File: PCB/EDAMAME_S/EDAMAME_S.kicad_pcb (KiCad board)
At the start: 2 copper layers, 75 x 96 mm, 73 parts, among them CN1 USB-B-MICRO, J1 Conn, J2 ISP, J3 Conn, J4 Nichrome, M1 Motor_L, M2 Motor_R, Q1 MTM231102LBF, Q2 2SC2712, SW1 power, U1 microSD, U2 ATMEGA1284P-MU, U3 LSM303C, U4 TPS63001, U5 GYSFDMAXB, U6 FT231XQ, U7 BD6211F, U8 INA226, U9 BD6211F, Y1 16MHz

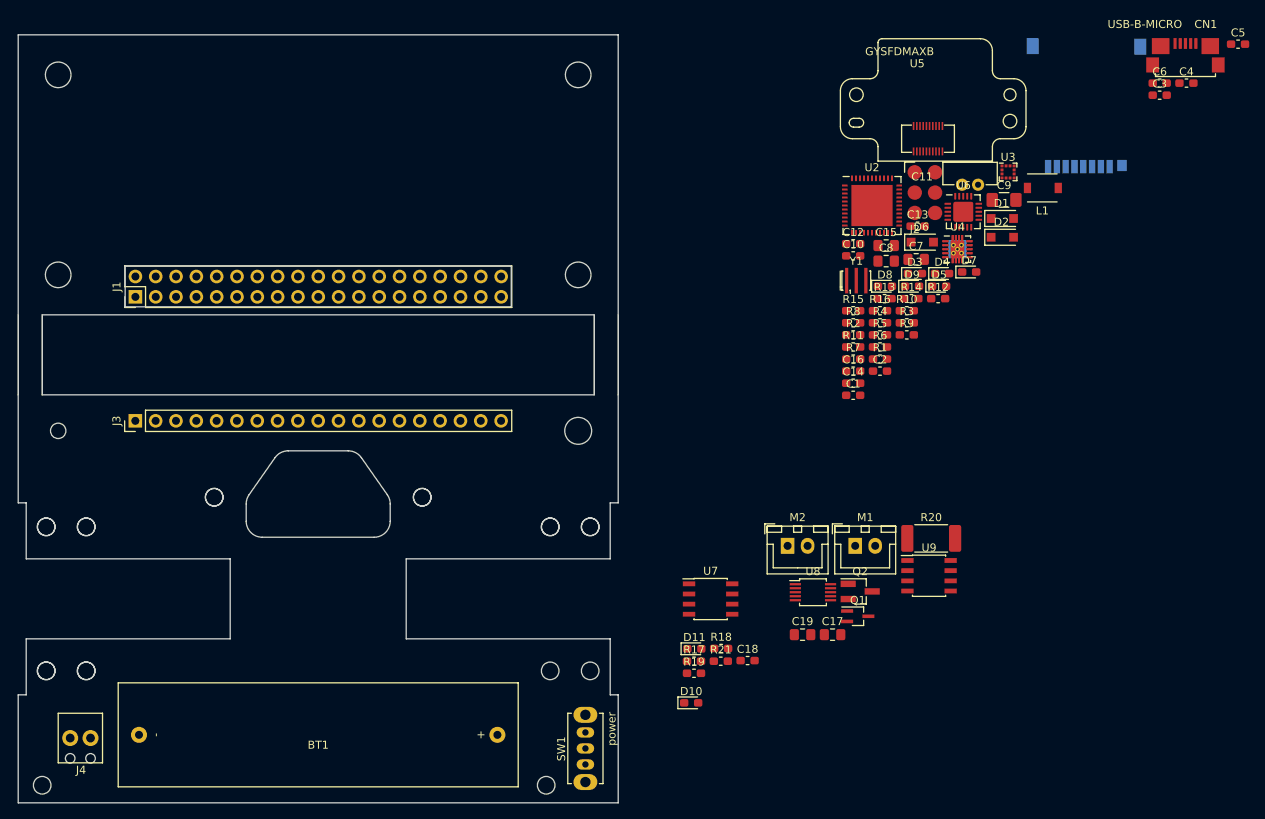
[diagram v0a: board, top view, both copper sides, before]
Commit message: えだまめS 基板更新
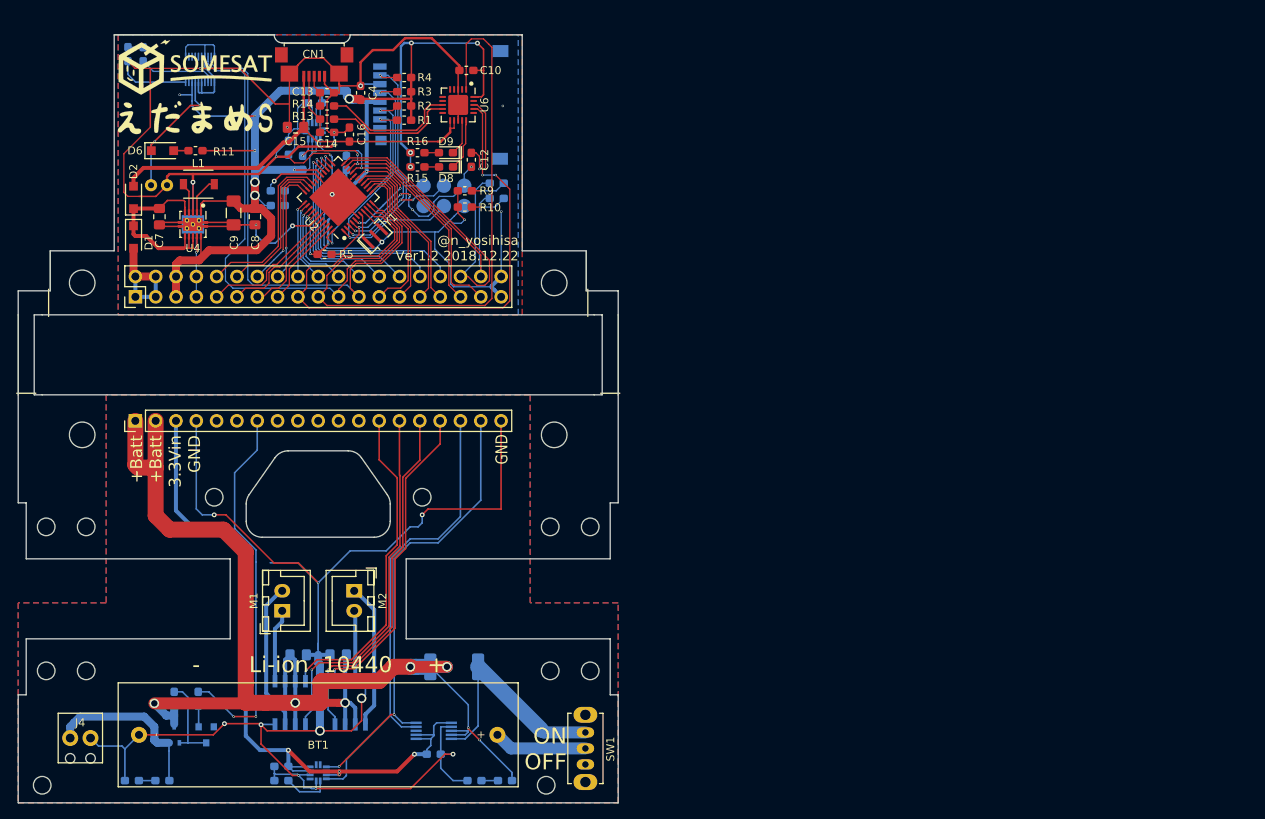
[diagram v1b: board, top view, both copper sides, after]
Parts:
- removed C1: 0.1u, Capacitor_SMD:C_0603_1608Metric_Pad1.05x0.95mm_HandSolder
- added C20: 0.1u, Capacitor_SMD:C_0603_1608Metric_Pad1.05x0.95mm_HandSolder, B.Cu at (61.4, 108.6)
- added C21: 0.1u, Capacitor_SMD:C_0603_1608Metric_Pad1.05x0.95mm_HandSolder, B.Cu at (61.4, 110.4)
- added G***: LOGO, logo:SOMESAT_edamame_s_logo, F.Cu at (50.6, 24.0)
- added G***: LOGO, logo:SOMESAT_logo, B.Cu at (83.5, 70.6)
- added U10: LSM303C, user:LGA-12_2x2mm_P0.5mm_HandSolder, B.Cu at (66.1, 109.4)
- C11, C18, C2, C3, C5, C6, D10, D11, D3, D4, D5, D7, J2, R12, R17, R18, R19, R20, R21, R6, R7, R8, U5, U8: moved to B.Cu
- C17: renamed from C19; moved to B.Cu
- C19: renamed from C17; moved to B.Cu
- M1: renamed from M2; value Motor_R -> Motor_L
- M2: renamed from M1; value Motor_L -> Motor_R
- Q1: footprint Package_TO_SOT_SMD:SOT-323_SC-70_Handsoldering -> Package_TO_SOT_SMD:SOT-323_SC-70; moved to B.Cu
- Q2: footprint Package_TO_SOT_SMD:SOT-23_Handsoldering -> Package_TO_SOT_SMD:SOT-23; moved to B.Cu
- U3: footprint Package_LGA:LGA-12_2x2mm_P0.5mm -> user:LGA-12_2x2mm_P0.5mm_HandSolder; moved to B.Cu
- U4: footprint Package_SON:Texas_S-PWSON-N10_ThermalVias -> Package_SON:Texas_S-PVSON-N10_ThermalVias
- U7: renamed from U9; moved to B.Cu
- U9: renamed from U7; moved to B.Cu
- Y1: footprint Crystal:Resonator_SMD_muRata_CSTxExxV-3Pin_3.0x1.1mm_HandSoldering -> Crystal:Resonator_SMD_muRata_CSTxExxV-3Pin_3.0x1.1mm
- moved C5 115.6 mm to (65.6, 25.7), turned to 180 degrees
- moved C6 109.2 mm to (62.3, 31.3), turned to 90 degrees
- moved CN1 108.9 mm to (65.6, 19.7), turned to 180 degrees
- moved D2 108.7 mm to (43.0, 37.5), turned to 90 degrees
- moved D1 108.6 mm to (43.0, 42.4), turned to 270 degrees
- moved D7 108.6 mm to (42.3, 19.6), turned to 90 degrees
- moved L1 105.5 mm to (51.1, 35.8)
- moved R12 104.0 mm to (44.2, 19.6), turned to 270 degrees
- moved C3 103.4 mm to (68.7, 38.1), turned to 180 degrees
- moved C4 103.2 mm to (71.4, 24.4), turned to 90 degrees
- moved C11 101.4 mm to (46.2, 36.0)
- moved C9 96.3 mm to (55.5, 39.4), turned to 270 degrees
- moved D6 95.7 mm to (46.6, 31.6)
- moved U4 95.6 mm to (50.4, 40.8), turned to 270 degrees
- moved C7 94.7 mm to (46.2, 39.9), turned to 270 degrees
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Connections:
- C14 pad 1: Net-(C13-Pad1) -> Net-(C14-Pad1)
- CN1 pad 2: Net-(C13-Pad1) -> Net-(C14-Pad1)
- CN1 pad 3: Net-(CN1-Pad3) -> Net-(C13-Pad1)
- CN1 pad 4: Net-(CN1-Pad4) -> (no net)
- D4 pad 1: GND -> Net-(D4-Pad1)
- D4 pad 2: Net-(D4-Pad2) -> /EDAMAME_S_core/19
- D5 pad 1: GND -> Net-(D5-Pad1)
- D5 pad 2: Net-(D5-Pad2) -> /EDAMAME_S_core/18
- J1 pad 1: Net-(J1-Pad1) -> Net-(D1-Pad2)
- J1 pad 10: /EDAMAME_S_core/18 -> /EDAMAME_S_core/A7
- J1 pad 12: /EDAMAME_S_core/19 -> /EDAMAME_S_core/A6
- J1 pad 14: /EDAMAME_S_core/20 -> /EDAMAME_S_core/A5
- J1 pad 16: /EDAMAME_S_core/21 -> /EDAMAME_S_core/A4
- J1 pad 18: /EDAMAME_S_core/22 -> /EDAMAME_S_core/A3
- J1 pad 20: /EDAMAME_S_core/23 -> /EDAMAME_S_core/A2
- J1 pad 22: /EDAMAME_S_core/A0 -> /EDAMAME_S_core/A1
- J1 pad 24: /EDAMAME_S_core/A1 -> /EDAMAME_S_core/A0
- J1 pad 26: /EDAMAME_S_core/A2 -> /EDAMAME_S_core/23
- J1 pad 28: /EDAMAME_S_core/A3 -> /EDAMAME_S_core/22
- J1 pad 3: Net-(J1-Pad1) -> Net-(D1-Pad2)
- J1 pad 30: /EDAMAME_S_core/A4 -> /EDAMAME_S_core/21
- J1 pad 32: /EDAMAME_S_core/A5 -> /EDAMAME_S_core/20
- J1 pad 34: /EDAMAME_S_core/A6 -> /EDAMAME_S_core/19
- J1 pad 36: /EDAMAME_S_core/A7 -> /EDAMAME_S_core/18
- J2 pad 2: +3V3 -> (no net)
- J3 pad 10: Net-(J3-Pad10) -> (no net)
- J3 pad 11: Net-(J3-Pad11) -> (no net)
- J3 pad 12: Net-(J3-Pad12) -> (no net)
- J3 pad 5: Net-(J3-Pad5) -> (no net)
- J3 pad 6: Net-(J3-Pad6) -> (no net)
- J3 pad 8: Net-(J3-Pad8) -> (no net)
- J3 pad 9: Net-(J3-Pad9) -> (no net)
- R10 pad 1: /EDAMAME_S_core/18 -> Net-(D5-Pad1)
- R10 pad 2: Net-(D5-Pad2) -> GND
- R13 pad 2: Net-(C13-Pad1) -> Net-(C14-Pad1)
- R14 pad 2: Net-(CN1-Pad3) -> Net-(C13-Pad1)
- R9 pad 1: /EDAMAME_S_core/19 -> Net-(D4-Pad1)
- R9 pad 2: Net-(D4-Pad2) -> GND
- U1 pad 1: Net-(U1-Pad1) -> (no net)
- U1 pad 8: Net-(U1-Pad8) -> (no net)
- U2 pad 29: Net-(U2-Pad29) -> (no net)
- U2 pad 45: (no net) -> GND
- U3 pad 11: Net-(U3-Pad11) -> (no net)
- U3 pad 12: Net-(U3-Pad12) -> (no net)
- U3 pad 7: Net-(U3-Pad7) -> (no net)
- U5 pad 4: Net-(U5-Pad4) -> (no net)
- U6 pad 10: Net-(U6-Pad10) -> (no net)
- U6 pad 16: Net-(U6-Pad16) -> (no net)
- U6 pad 19: Net-(U6-Pad19) -> (no net)
- U6 pad 2: Net-(U6-Pad2) -> (no net)
- U6 pad 4: Net-(U6-Pad4) -> (no net)
- U6 pad 5: Net-(U6-Pad5) -> (no net)
- U6 pad 6: Net-(U6-Pad6) -> (no net)
- U6 pad 7: Net-(U6-Pad7) -> (no net)
- U7 pad 4: /EDAMAME_S_Ex/MOTOR_RR -> /EDAMAME_S_Ex/MOTOR_LF
- U7 pad 5: /EDAMAME_S_Ex/MOTOR_RF -> /EDAMAME_S_Ex/MOTOR_LR
- U8 pad 3: Net-(U8-Pad3) -> (no net)
- U9 pad 4: /EDAMAME_S_Ex/MOTOR_LF -> /EDAMAME_S_Ex/MOTOR_RR
- U9 pad 5: /EDAMAME_S_Ex/MOTOR_LR -> /EDAMAME_S_Ex/MOTOR_RF
- Y1 pad 2: Net-(Y1-Pad2) -> GND
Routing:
- net GND: track 0.00 -> 313.1 mm, vias 0 -> 18
- net +3V3: track 0.00 -> 207.7 mm, vias 0 -> 18
- net GNDPWR: track 0.00 -> 195.7 mm, vias 0 -> 10
- net +BATT: track 0.00 -> 159.3 mm, vias 0 -> 7
- net VCC: track 0.00 -> 92.1 mm, vias 0 -> 4
- net /EDAMAME_S_core/AVR→PC: track 0.00 -> 83.5 mm
- net /EDAMAME_S_core/PC→AVR: track 0.00 -> 76.8 mm, vias 0 -> 2
- net /EDAMAME_S_core/AVR→GPS: track 0.00 -> 68.1 mm
- net /EDAMAME_S_core/GPS→AVR: track 0.00 -> 66.2 mm
- net /EDAMAME_S_Ex/SDA: track 0.00 -> 58.9 mm
- net /EDAMAME_S_Ex/SCL: track 0.00 -> 57.7 mm, vias 0 -> 2
- net +5V: track 0.00 -> 53.7 mm
- net /EDAMAME_S_Ex/Nichrome: track 0.00 -> 47.7 mm, vias 0 -> 2
- net /EDAMAME_S_Ex/MOTOR_LR: track 0.00 -> 45.3 mm, vias 0 -> 1
- net /EDAMAME_S_Ex/MOTOR_RR: track 0.00 -> 44.6 mm, vias 0 -> 1
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- added copper zone on B.Cu, net GND
- added copper zone on F.Cu, net GND
- added copper zone on B.Cu, net GNDPWR
- added copper zone on F.Cu, net GNDPWR
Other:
- outline, holes or cut-outs redrawn
- rule via_min_drill: 0.3 -> 0.2
- rule via_min_size: 0.6048 -> 0.3
- board text added: "+Batt +Batt 3.3Vin GND"
- board text added: "- Li-ion 10440 +"
- board text added: "@n_yosihisa Ver1.2 2018.12.22"
- board text added: "EDAMAME S @n_yosihisa Ver1.2 2018.12.22"
- board text added: "GND"
- board text added: "ISP"
- board text added: "ON OFF"
- board text added: "Vin Vin 3.3V GND"

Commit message: Add flightpin
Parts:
- added J5: FlightPin, Connector_PinHeader_2.54mm:PinHeader_1x02_P2.54mm_Horizontal, F.Cu at (39.1, 73.8)
- added R22: 10K, Resistor_SMD:R_0603_1608Metric_Pad1.05x0.95mm_HandSolder, B.Cu at (43.9, 73.8)
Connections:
- J3 pad 5: (no net) -> /EDAMAME_S_Ex/FlightPin
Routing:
- net GNDPWR: track 195.7 -> 278.2 mm
- net /EDAMAME_S_Ex/FlightPin: track 0.00 -> 21.9 mm, vias 0 -> 1
- net VCC: track 92.1 -> 96.1 mm
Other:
- board text added: "@n_yosihisa Ver1.2 2018.12.23"
- board text added: "EDAMAME S @n_yosihisa Ver1.2 2018.12.23"
- board text removed: "@n_yosihisa Ver1.2 2018.12.22"
- board text removed: "EDAMAME S @n_yosihisa Ver1.2 2018.12.22"

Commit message: EdamameS_V1.10
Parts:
- removed C15, C17, C19: 10u, Capacitor_SMD:C_0805_2012Metric_Pad1.15x1.40mm_HandSolder
- removed C16, C18, C20, C21: 0.1u, Capacitor_SMD:C_0603_1608Metric_Pad1.05x0.95mm_HandSolder
- removed D10: Nichrome, LED_SMD:LED_0603_1608Metric_Pad1.05x0.95mm_HandSolder
- removed D11: POWER, LED_SMD:LED_0603_1608Metric_Pad1.05x0.95mm_HandSolder
- removed D8: TX_LED, LED_SMD:LED_0603_1608Metric_Pad1.05x0.95mm_HandSolder
- removed D9: RX_LED, LED_SMD:LED_0603_1608Metric_Pad1.05x0.95mm_HandSolder
- removed the G*** at (50.6, 24.0)
- removed the G*** at (83.5, 70.6)
- removed J3: Conn, Connector_PinHeader_2.54mm:PinHeader_1x19_P2.54mm_Vertical
- removed J4: Nichrome, user:MPT0.5_2-2.54
- removed L1: 2.2uH, user:inductor_VLF4012-2R2
- removed R15, R16: 1k, Resistor_SMD:R_0603_1608Metric_Pad1.05x0.95mm_HandSolder
- removed R17, R19, R22: 10K, Resistor_SMD:R_0603_1608Metric_Pad1.05x0.95mm_HandSolder
- removed R18, R21: 1K, Resistor_SMD:R_0603_1608Metric_Pad1.05x0.95mm_HandSolder
- removed R20: 10m, Resistor_SMD:R_2512_6332Metric_Pad1.52x3.35mm_HandSolder
- removed U10: LSM303C, user:LGA-12_2x2mm_P0.5mm_HandSolder
- removed Y1: 16MHz, Crystal:Resonator_SMD_muRata_CSTxExxV-3Pin_3.0x1.1mm
- added BT2: 10440, user:BH-411, F.Cu at (68.6, 93.7)
- added BT3: 10440, user:BH-411, F.Cu at (68.6, 69.2)
- added C1: 0.1u, Capacitors_SMD:C_0603_HandSoldering, B.Cu at (92.1, 51.7)
- added G***: LOGO, mod:SOMESAT_LOGO, B.Cu at (74.5, 97.7)
- added G***: LOGO, mod:SOMESAT_LOGO, F.Cu at (57.3, 50.4)
- added J6: CHARGE, EH:S3B-EH, B.Cu at (53.4, 101.9)
- added Q3: 2SC2712, TO_SOT_Packages_SMD:SOT-23_Handsoldering, B.Cu at (91.8, 83.2)
- BT1: value 10440 -> BACKUP; footprint user:BH-411 -> user:MS621FE_FL11E; moved to B.Cu
- C10: value 0.1u -> 100u; footprint Capacitor_SMD:C_0603_1608Metric_Pad1.05x0.95mm_HandSolder -> Capacitors_SMD:C_1206_HandSoldering; moved to B.Cu
- C11: value 0.22F 3.3V -> 10u; footprint user:MS621FE_FL11E -> Capacitors_SMD:C_1206_HandSoldering
- C12: footprint Capacitor_SMD:C_0603_1608Metric_Pad1.05x0.95mm_HandSolder -> Capacitors_SMD:C_0603_HandSoldering; moved to B.Cu
- C13: value 47p -> 10u; footprint Capacitor_SMD:C_0603_1608Metric_Pad1.05x0.95mm_HandSolder -> Capacitors_SMD:C_1206_HandSoldering; moved to B.Cu
- C14: value 47p -> 10u; footprint Capacitor_SMD:C_0603_1608Metric_Pad1.05x0.95mm_HandSolder -> Capacitors_SMD:C_0603_HandSoldering; moved to B.Cu
- C2, C5: footprint Capacitor_SMD:C_0603_1608Metric_Pad1.05x0.95mm_HandSolder -> Capacitors_SMD:C_0603_HandSoldering
- C3: value 0.1u -> 47p; footprint Capacitor_SMD:C_0603_1608Metric_Pad1.05x0.95mm_HandSolder -> Capacitors_SMD:C_0603_HandSoldering
- C4: value 0.1u -> 47p; footprint Capacitor_SMD:C_0603_1608Metric_Pad1.05x0.95mm_HandSolder -> Capacitors_SMD:C_0603_HandSoldering; moved to B.Cu
- C6: value 0.1u -> 10u; footprint Capacitor_SMD:C_0603_1608Metric_Pad1.05x0.95mm_HandSolder -> Capacitors_SMD:C_0603_HandSoldering
- C7, C8: value 10u -> 0.1u; footprint Capacitor_SMD:C_0805_2012Metric_Pad1.15x1.40mm_HandSolder -> Capacitors_SMD:C_0603_HandSoldering; moved to B.Cu
- C9: value 100u -> 0.1u; footprint Capacitor_SMD:C_1206_3216Metric_Pad1.42x1.75mm_HandSolder -> Capacitors_SMD:C_0603_HandSoldering; moved to B.Cu
- CN1: footprint user:Micro-USB -> mylib:Micro-USB; moved to B.Cu
- D1: value GS1010FL -> TXLED; footprint Diode_SMD:D_SOD-123F -> LEDs:LED_0603_HandSoldering; moved to B.Cu
- D2: value GS1010FL -> RXLED; footprint Diode_SMD:D_SOD-123F -> LEDs:LED_0603_HandSoldering; moved to B.Cu
- D3: value POWER -> GS1010FL; footprint LED_SMD:LED_0603_1608Metric_Pad1.05x0.95mm_HandSolder -> Diodes_SMD:D_SOD-123F
- D4: value LED1 -> GS1010FL; footprint LED_SMD:LED_0603_1608Metric_Pad1.05x0.95mm_HandSolder -> Diodes_SMD:D_SOD-123F
- D5: value LED2 -> GS1010FL; footprint LED_SMD:LED_0603_1608Metric_Pad1.05x0.95mm_HandSolder -> Diodes_SMD:D_SOD-123F
- D6: value GS1010FL -> Nichrome; footprint Diode_SMD:D_SOD-123F -> LEDs:LED_0603_HandSoldering; moved to B.Cu
- D7: value 1PPS -> POWER; footprint LED_SMD:LED_0603_1608Metric_Pad1.05x0.95mm_HandSolder -> LEDs:LED_0603_HandSoldering
- J1: value Conn -> Conn_01x20; footprint Connector_PinHeader_2.54mm:PinHeader_2x19_P2.54mm_Vertical -> Socket_Strips:Socket_Strip_Straight_1x20_Pitch2.54mm; moved to B.Cu
- J2: value ISP -> Conn_01x20; footprint user:AVR_ISP -> Socket_Strips:Socket_Strip_Straight_1x20_Pitch2.54mm; moved to F.Cu
- J5: value FlightPin -> Nichrome; footprint Connector_PinHeader_2.54mm:PinHeader_1x02_P2.54mm_Horizontal -> user:MPT0.5_2-2.54
- M1, M2: footprint Connector_JST:JST_XH_B02B-XH-A_1x02_P2.50mm_Vertical -> EH:B2B-EH
- Q1: value MTM231102LBF -> NDS9936; footprint Package_TO_SOT_SMD:SOT-323_SC-70 -> Housings_SOIC:SOIC-8_3.9x4.9mm_Pitch1.27mm
- Q2: value 2SC2712 -> FDS4675; footprint Package_TO_SOT_SMD:SOT-23 -> Housings_SOIC:SOIC-8_3.9x4.9mm_Pitch1.27mm
- R1: value 10k -> 10K; footprint Resistor_SMD:R_0603_1608Metric_Pad1.05x0.95mm_HandSolder -> Resistors_SMD:R_0603_HandSoldering; moved to B.Cu
- R10: value 1k -> 1K; footprint Resistor_SMD:R_0603_1608Metric_Pad1.05x0.95mm_HandSolder -> Resistors_SMD:R_0603_HandSoldering; moved to B.Cu
- R11: value 100 -> 10K; footprint Resistor_SMD:R_0603_1608Metric_Pad1.05x0.95mm_HandSolder -> Resistors_SMD:R_0603_HandSoldering; moved to B.Cu
- R12: value 1k -> 10m; footprint Resistor_SMD:R_0603_1608Metric_Pad1.05x0.95mm_HandSolder -> Resistors_SMD:R_2512_HandSoldering
- R13: value 33 -> 1K; footprint Resistor_SMD:R_0603_1608Metric_Pad1.05x0.95mm_HandSolder -> Resistors_SMD:R_0603_HandSoldering; moved to B.Cu
- R14: value 33 -> 10K; footprint Resistor_SMD:R_0603_1608Metric_Pad1.05x0.95mm_HandSolder -> Resistors_SMD:R_0603_HandSoldering; moved to B.Cu
- R2, R3: value 10k -> 33; footprint Resistor_SMD:R_0603_1608Metric_Pad1.05x0.95mm_HandSolder -> Resistors_SMD:R_0603_HandSoldering; moved to B.Cu
- R4, R5: value 10k -> 1K; footprint Resistor_SMD:R_0603_1608Metric_Pad1.05x0.95mm_HandSolder -> Resistors_SMD:R_0603_HandSoldering; moved to B.Cu
- R6, R7: value 2.2k -> 2.2K; footprint Resistor_SMD:R_0603_1608Metric_Pad1.05x0.95mm_HandSolder -> Resistors_SMD:R_0603_HandSoldering
- R8: value 1k -> 100; footprint Resistor_SMD:R_0603_1608Metric_Pad1.05x0.95mm_HandSolder -> Resistors_SMD:R_0603_HandSoldering
- R9: value 1k -> 10K; footprint Resistor_SMD:R_0603_1608Metric_Pad1.05x0.95mm_HandSolder -> Resistors_SMD:R_0603_HandSoldering; moved to B.Cu
- SW1: footprint user:SS-12D01-VG4 -> mylib:SS-12D01-VG4
- U2: value ATMEGA1284P-MU -> FT231XS; footprint Package_DFN_QFN:QFN-44-1EP_7x7mm_P0.5mm_EP5.15x5.15mm -> SMD_Packages:SSOP-20; moved to B.Cu
- U3: value LSM303C -> ESP32-WROOM; footprint user:LGA-12_2x2mm_P0.5mm_HandSolder -> ESP32-footprints-Lib:ESP32-WROOM
- U4: value TPS63001 -> NJM2391DL1-33; footprint Package_SON:Texas_S-PVSON-N10_ThermalVias -> TO_SOT_Packages_SMD:TO-252-2_Rectifier; moved to B.Cu
- U5: value GYSFDMAXB -> LSM303C; footprint user:GYSFDMAXB -> Housings_LGA:LGA-12_2x2mm_Pitch0.5mm
- U6: value FT231XQ -> GPS-54D; footprint Package_DFN_QFN:QFN-20-1EP_4x4mm_P0.5mm_EP2.5x2.5mm -> user:GPS-54
- U7, U9: value BD6211F -> BD6231F; footprint Package_SO:SOIC-8_3.9x4.9mm_P1.27mm -> Housings_SOIC:SOIC-8_3.9x4.9mm_Pitch1.27mm
- U8: footprint Package_SO:MSOP-10_3x3mm_P0.5mm -> Housings_SSOP:MSOP-10_3x3mm_Pitch0.5mm
- moved D6 91.3 mm to (105.2, 101.6), turned to 180 degrees
- moved BT1 84.2 mm to (90.8, 24.1), turned to 180 degrees
- moved Q1 75.4 mm to (96.6, 47.0)
- moved SW1 68.3 mm to (31.6, 98.2)
- moved J5 68.2 mm to (102.2, 99.7), turned to 0 degrees
- moved R10 65.0 mm to (100.6, 101.6), turned to 0 degrees
- moved R12 61.9 mm to (37.6, 81.2), turned to 180 degrees
- moved R11 61.1 mm to (89.8, 78.6)
- moved C12 59.5 mm to (52.7, 82.6)
- moved Q2 52.2 mm to (99.7, 83.2), turned to 0 degrees
- moved R13 50.6 mm to (31.0, 63.0), turned to 270 degrees
- moved D7 48.9 mm to (31.0, 67.2)
- moved C11 47.9 mm to (79.4, 70.5), turned to 270 degrees
- moved C13 46.8 mm to (59.0, 70.5), turned to 270 degrees
- moved R9 43.5 mm to (95.9, 78.6), turned to 0 degrees
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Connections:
- BT1 pad 2: GNDPWR -> GND
- C11 pad 1: Net-(C11-Pad1) -> +BATT
- C11 pad 2: GND -> GNDPWR
- C12 pad 1: Net-(C12-Pad1) -> VCC
- C12 pad 2: /EDAMAME_S_core/RST -> GNDPWR
- C13 pad 1: Net-(C13-Pad1) -> +BATT
- C13 pad 2: GND -> GNDPWR
- C14 pad 1: Net-(C14-Pad1) -> /EN
- C3 pad 1: +3V3 -> Net-(C3-Pad1)
- C4 pad 1: +3V3 -> Net-(C4-Pad1)
- C5 pad 1: +3V3 -> +5V
- C6 pad 1: Net-(C6-Pad1) -> +5V
- C7 pad 1: Net-(C7-Pad1) -> +3V3
- C8 pad 1: +3V3 -> Net-(C8-Pad1)
- C9 pad 1: +3V3 -> Net-(C9-Pad1)
- CN1 pad 2: Net-(C14-Pad1) -> Net-(C4-Pad1)
- CN1 pad 3: Net-(C13-Pad1) -> Net-(C3-Pad1)
- D1 pad 1: Net-(C7-Pad1) -> Net-(D1-Pad1)
- D2 pad 1: Net-(C7-Pad1) -> Net-(D2-Pad1)
- D2 pad 2: +5V -> Net-(D2-Pad2)
- D3 pad 1: GND -> Net-(C9-Pad1)
- D3 pad 2: Net-(D3-Pad2) -> +5V
- D4 pad 1: Net-(D4-Pad1) -> Net-(C9-Pad1)
- D4 pad 2: /EDAMAME_S_core/19 -> VDC
- D5 pad 2: /EDAMAME_S_core/18 -> +3V3
- D6 pad 1: Net-(C11-Pad1) -> GNDPWR
- D7 pad 1: GND -> GNDPWR
- J1 pad 1: Net-(D1-Pad2) -> VDC
- J1 pad 10: /EDAMAME_S_core/A7 -> /IO35
- J1 pad 11: /EDAMAME_S_core/1 -> /IO32
- J1 pad 12: /EDAMAME_S_core/A6 -> /IO33
- J1 pad 13: /EDAMAME_S_core/2 -> /IO25
- J1 pad 14: /EDAMAME_S_core/A5 -> /IO26
- J1 pad 15: /EDAMAME_S_core/3- -> /IO27
- J1 pad 16: /EDAMAME_S_core/A4 -> /IO14
- J1 pad 17: /EDAMAME_S_core/PC→AVR -> /IO13
- J1 pad 18: /EDAMAME_S_core/A3 -> /I2C_SDA
- J1 pad 19: /EDAMAME_S_core/AVR→PC -> /I2C_SCL
- J1 pad 2: Net-(D1-Pad2) -> VDC
- J1 pad 20: /EDAMAME_S_core/A2 -> GND
- J1 pad 3: Net-(D1-Pad2) -> +3V3
- J1 pad 4: Net-(D1-Pad2) -> +3V3
- J1 pad 5: +3V3 -> GND
- J1 pad 6: +3V3 -> GND
- J1 pad 7: GND -> /S_VP
- J1 pad 8: GND -> /S_VN
- J1 pad 9: /EDAMAME_S_core/0 -> /IO34
- J2 pad 1: /EDAMAME_S_core/MISO -> +BATT
- J2 pad 2: (no net) -> +BATT
- J2 pad 3: /EDAMAME_S_core/SCK -> VCC
- J2 pad 4: /EDAMAME_S_core/MOSI -> VCC
- J2 pad 5: /EDAMAME_S_core/RST -> GNDPWR
- J2 pad 6: GND -> GNDPWR
- J5 pad 1: /EDAMAME_S_Ex/FlightPin -> Net-(J5-Pad1)
- Q1 pad 1: Net-(Q1-Pad1) -> /DTR
- Q1 pad 2: Net-(J4-Pad1) -> /RST
- Q1 pad 3: +BATT -> /RST
- Q2 pad 1: Net-(Q2-Pad1) -> +BATT
- Q2 pad 2: GNDPWR -> +BATT
- Q2 pad 3: Net-(Q1-Pad1) -> +BATT
- R1 pad 1: /EDAMAME_S_core/SS -> +3V3
- R1 pad 2: +3V3 -> /SPI_MISO
- R10 pad 1: Net-(D5-Pad1) -> Net-(J5-Pad1)
- R10 pad 2: GND -> Net-(D6-Pad2)
- R11 pad 1: +3V3 -> Net-(Q3-Pad1)
- R11 pad 2: Net-(D6-Pad2) -> /Nichrome
- R12 pad 1: Net-(D7-Pad2) -> +BATT
- R13 pad 1: Net-(R13-Pad1) -> +BATT
- R13 pad 2: Net-(C14-Pad1) -> Net-(D7-Pad2)
- R14 pad 1: Net-(R14-Pad1) -> /EN
- R14 pad 2: Net-(C13-Pad1) -> +3V3
- R2 pad 1: /EDAMAME_S_core/MOSI -> Net-(R2-Pad1)
- R2 pad 2: +3V3 -> Net-(C4-Pad1)
- R3 pad 1: /EDAMAME_S_core/SCK -> Net-(R3-Pad1)
- R3 pad 2: +3V3 -> Net-(C3-Pad1)
- R4 pad 1: /EDAMAME_S_core/MISO -> +3V3
- R4 pad 2: +3V3 -> Net-(D1-Pad2)
- R5 pad 2: /EDAMAME_S_core/RST -> Net-(D2-Pad2)
- R6 pad 1: +3V3 -> /I2C_SDA
- R6 pad 2: /EDAMAME_S_core/I2C_SDA -> +3V3
- R7 pad 1: +3V3 -> /I2C_SCL
- R7 pad 2: /EDAMAME_S_core/I2C_SCL -> +3V3
- R8 pad 1: Net-(D3-Pad2) -> Net-(BT1-Pad1)
- R8 pad 2: +3V3 -> Net-(D5-Pad1)
- R9 pad 1: Net-(D4-Pad1) -> Net-(Q2-Pad4)
- R9 pad 2: GND -> +BATT
- SW1 pad 1: Net-(R20-Pad2) -> Net-(R12-Pad2)
- SW1 pad 2: Net-(BT1-Pad1) -> Net-(BT2-Pad1)
- U1 pad 2: /EDAMAME_S_core/SS -> /SPI_CS
- U1 pad 3: /EDAMAME_S_core/MOSI -> /SPI_MOSI
- U1 pad 5: /EDAMAME_S_core/SCK -> /SPI_SCLK
- U1 pad 7: /EDAMAME_S_core/MISO -> /SPI_MISO
- U2 pad 1: /EDAMAME_S_core/MOSI -> /DTR
- U2 pad 10: /EDAMAME_S_core/AVR→PC -> Net-(D2-Pad1)
- U2 pad 11: /EDAMAME_S_core/GPS→AVR -> Net-(R3-Pad1)
- U2 pad 12: /EDAMAME_S_core/AVR→GPS -> Net-(R2-Pad1)
- U2 pad 13: /EDAMAME_S_core/12- -> (no net)
- U2 pad 14: /EDAMAME_S_core/13- -> +5V
- U2 pad 15: /EDAMAME_S_core/14- -> +5V
- U2 pad 16: /EDAMAME_S_core/15- -> GND
- U2 pad 17: +3V3 -> Net-(D1-Pad1)
- U2 pad 18: GND -> (no net)
- U2 pad 19: /EDAMAME_S_core/I2C_SCL -> (no net)
- U2 pad 2: /EDAMAME_S_core/MISO -> /RST
- U2 pad 20: /EDAMAME_S_core/I2C_SDA -> /PC→ESP32
- U2 pad 3: /EDAMAME_S_core/SCK -> +3V3
- U2 pad 4: /EDAMAME_S_core/RST -> /ESP32→PC
- U2 pad 5: +3V3 -> (no net)
- U2 pad 7: Net-(U2-Pad7) -> (no net)
- U2 pad 8: Net-(U2-Pad8) -> (no net)
- U2 pad 9: /EDAMAME_S_core/PC→AVR -> (no net)
- U3 pad 1: /EDAMAME_S_core/I2C_SCL -> GND
- U3 pad 10: +3V3 -> /IO25
- U3 pad 11: (no net) -> /IO26
- U3 pad 12: (no net) -> /IO27
- U3 pad 3: +3V3 -> /EN
- U3 pad 4: /EDAMAME_S_core/I2C_SDA -> /S_VP
- U3 pad 5: Net-(C6-Pad1) -> /S_VN
- U3 pad 6: GND -> /IO34
- U3 pad 7: (no net) -> /IO35
- U3 pad 8: GND -> /IO32
- U3 pad 9: +3V3 -> /IO33
- U4 pad 1: +3V3 -> Net-(C9-Pad1)
- U4 pad 2: Net-(L1-Pad2) -> GND
- U4 pad 3: GND -> +3V3
- U5 pad 1: GND -> /I2C_SCL
- U5 pad 10: GND -> +3V3
- U5 pad 12: GND -> (no net)
- U5 pad 2: GND -> +3V3
- U5 pad 3: /EDAMAME_S_core/AVR→GPS -> +3V3
- U5 pad 4: (no net) -> /I2C_SDA
- U5 pad 5: /EDAMAME_S_core/GPS→AVR -> Net-(C8-Pad1)
- U5 pad 6: Net-(R12-Pad2) -> GND
- U5 pad 7: GND -> (no net)
- U5 pad 8: (no net) -> GND
- U5 pad 9: (no net) -> +3V3
- U6 pad 1: /EDAMAME_S_core/AVR→PC -> /ESP32→GPS
- U6 pad 2: (no net) -> GND
- U6 pad 3: GND -> /GPS→ESP32
- U6 pad 4: (no net) -> Net-(BT1-Pad1)
- U6 pad 5: (no net) -> +3V3
- U6 pad 8: Net-(R14-Pad1) -> (no net)
- U7 pad 4: /EDAMAME_S_Ex/MOTOR_LF -> /MOTOR_LF
- U7 pad 5: /EDAMAME_S_Ex/MOTOR_LR -> /MOTOR_LR
- U8 pad 10: Net-(R20-Pad2) -> Net-(R12-Pad2)
- U8 pad 4: /EDAMAME_S_Ex/SDA -> /SDA
- U8 pad 5: /EDAMAME_S_Ex/SCL -> /SCL
- U9 pad 4: /EDAMAME_S_Ex/MOTOR_RR -> /MOTOR_RR
- U9 pad 5: /EDAMAME_S_Ex/MOTOR_RF -> /MOTOR_RF
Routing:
- net GNDPWR: track 278.2 -> 71.1 mm, vias 10 -> 4
- net /EN: track 0.00 -> 101.2 mm, vias 0 -> 2
- net GND: track 313.1 -> 212.6 mm, vias 18 -> 11
- net /EDAMAME_S_core/AVR→PC: track 83.5 -> 0.00 mm
- net /EDAMAME_S_core/PC→AVR: track 76.8 -> 0.00 mm, vias 2 -> 0
- net /I2C_SCL: track 0.00 -> 74.9 mm, vias 0 -> 2
- net /EDAMAME_S_core/AVR→GPS: track 68.1 -> 0.00 mm
- net /EDAMAME_S_core/GPS→AVR: track 66.2 -> 0.00 mm
- net /I2C_SDA: track 0.00 -> 66.1 mm, vias 0 -> 2
- net Net-(BT2-Pad2): track 0.00 -> 65.7 mm
- net /EDAMAME_S_Ex/SDA: track 58.9 -> 0.00 mm
- net /EDAMAME_S_Ex/SCL: track 57.7 -> 0.00 mm, vias 2 -> 0
- net /SCL: track 0.00 -> 55.8 mm, vias 0 -> 1
- net /SDA: track 0.00 -> 54.8 mm, vias 0 -> 1
- net /BOOT: track 0.00 -> 54.3 mm, vias 0 -> 2
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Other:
- board size 75 x 96 mm -> 80 x 87 mm
- rule via_min_drill: 0.2 -> 0.3
- rule via_min_size: 0.3 -> 0.6048
- board text added: "+ -"
- board text added: "@n_yosihisa 2018.6.18 EDAMAME S Extension Board"
- board text added: "EDAMAME S Bus Board Prototype @n_yosihisa 2018.6.18"
- board text added: "OFF ON"
- board text added: "Vin Vin 3.3V 3.3V GND GND 36/A0 (input only) 39/A3 (input only) 34/A6 (input only) 35/A7 (input only) 32/A4/T9 33/A5/T8 25/A18/DAC_1 26/A19/DAC_2 27/A17/T7 14/A16/T6 13/A14/T4 21/SDA 22/SCL GND"
- board text removed: "+Batt +Batt 3.3Vin GND"
- board text removed: "- Li-ion 10440 +"
- board text removed: "@n_yosihisa Ver1.2 2018.12.23"
- board text removed: "EDAMAME S @n_yosihisa Ver1.2 2018.12.23"
- board text removed: "GND"
- board text removed: "ISP"
- board text removed: "ON OFF"
- board text removed: "Vin Vin 3.3V GND"
